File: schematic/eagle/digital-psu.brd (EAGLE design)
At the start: 107.6 x 85.1 mm, 79 parts, among them IC1 TL072P, IC2 TLC272P, Q1 MPSA56-TO92, T3 2N3055, T4 2N3055, T5 2N3055, X1 Vout, X2 PASS_TRANSISTORS, X3 AC_IN

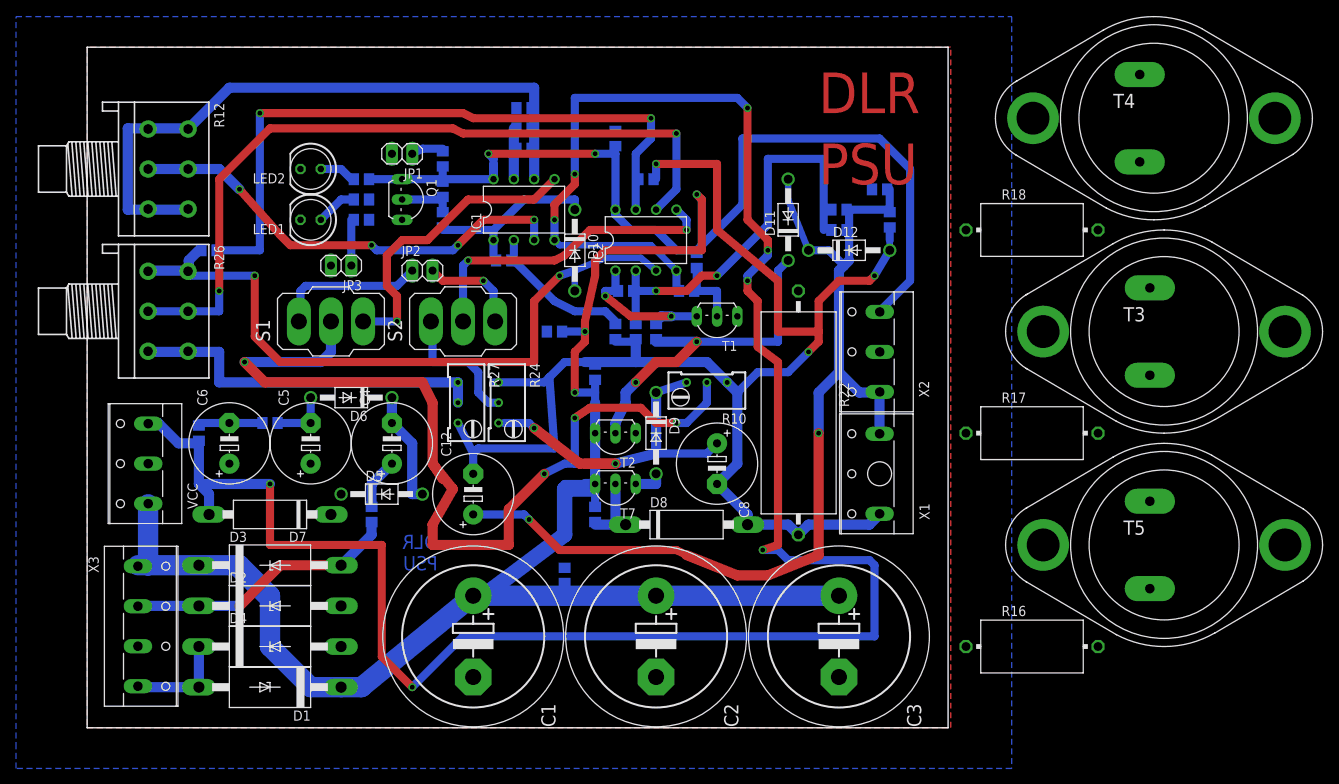
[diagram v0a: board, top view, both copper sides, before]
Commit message: removed all airwires
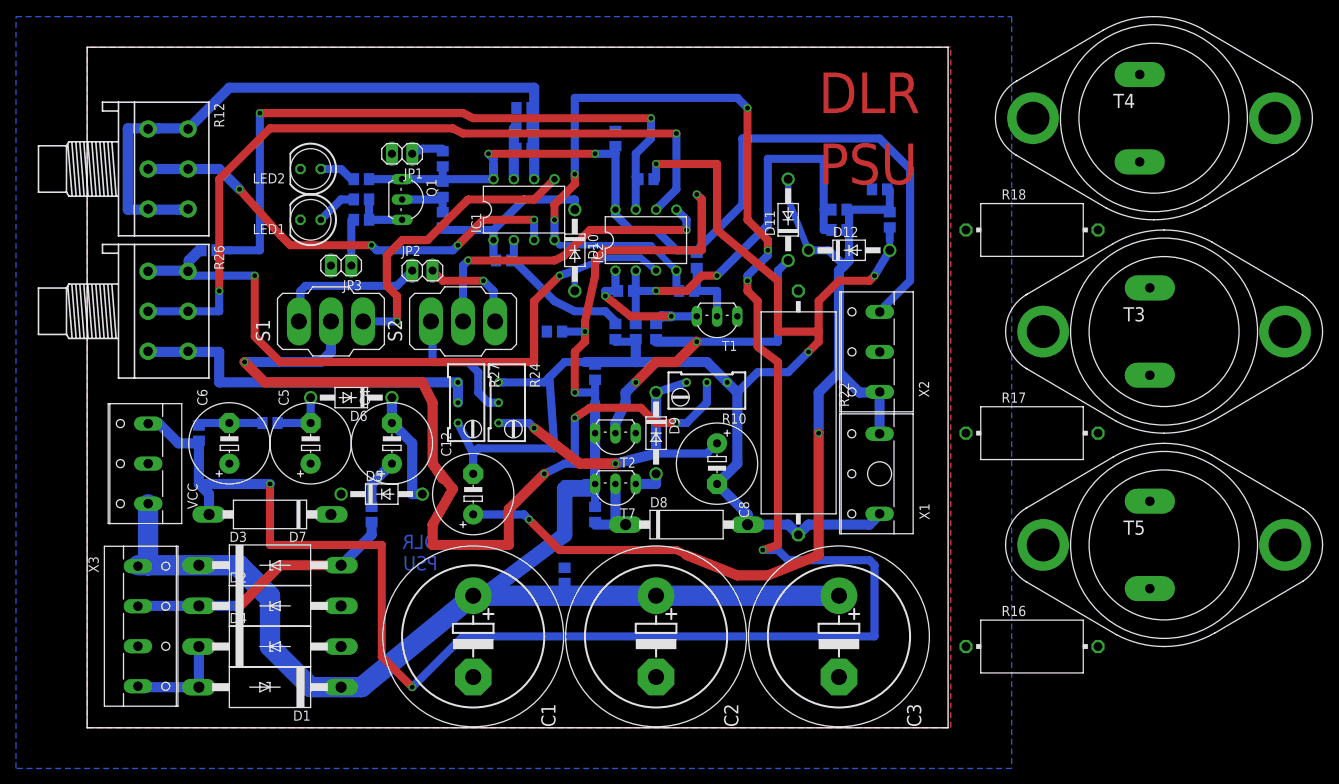
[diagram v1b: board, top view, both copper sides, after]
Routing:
- net N$20: track 82.1 -> 95.1 mm
- net ADJ_VOLT: track 79.8 -> 88.9 mm
- net N$41: track 124.4 -> 131.2 mm
- net N$11: track 0.00 -> 6.67 mm
- net N$36: track 45.1 -> 50.3 mm
- net VCC: track 362.5 -> 366.3 mm
- net N$23: track 6.35 -> 9.34 mm
- net N$38: track 50.4 -> 53.0 mm
- net VNEG: track 272.2 -> 274.1 mm
- net N$1: track 34.2 -> 35.8 mm
- net N$16: track 7.62 -> 9.21 mm
- net N$3: track 12.7 -> 14.0 mm
- net N$17: track 7.62 -> 8.89 mm
- net GND_HIGHER: track 173.1 -> 174.1 mm
- net N$30: track 83.5 -> 84.3 mm
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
